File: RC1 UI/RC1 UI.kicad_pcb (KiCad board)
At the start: 2 copper layers, 99.1 x 97.2 mm, 59 parts, among them J1 KEYPAD, J2 RC1_UI_Port, J3 COM, J4 TAPE, M1 Mounting, M2 Mounting, M3 Mounting, M4 Mounting, Q1 2N3904, Q2 2N3904, Q3 2N3904, Q4 2N3904, Q5 2N3904, Q6 2N3904, U1 74LS138, U2 74LS138, U3 74LS01, U4 74LS00, U5 74LS04, U6 74LS244

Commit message: Gerber export
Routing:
- net VCC: track 411.6 -> 409.4 mm
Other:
- outline, holes or cut-outs redrawn
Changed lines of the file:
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@@
     (links 202)
     (no_connects 0)
-    (area 107.874999 36.754999 207.085001 134.060001)
+    (area 104.775 34.925 215.880001 140.970001)
     (thickness 1.6)
-    (drawings 147)
-    (tracks 1225)
+    (drawings 149)
+    (tracks 1228)
     (zones 0)
     (modules 59)
@@
     )
   )
+  (gr_line (start 202.565 133.985) (end 112.395 133.985) (angle 90) (layer Edge.Cuts) (width 0.15))
+  (gr_line (start 207.01 41.275) (end 207.01 129.54) (angle 90) (layer Edge.Cuts) (width 0.15))
+  (gr_line (start 107.95 129.54) (end 107.95 41.275) (angle 90) (layer Edge.Cuts) (width 0.15))
+  (gr_arc (start 202.565 129.54) (end 207.01 129.54) (angle 90) (layer Edge.Cuts) (width 0.15))
+  (gr_arc (start 112.395 129.54) (end 112.395 133.985) (angle 90) (layer Edge.Cuts) (width 0.15))
   (gr_text "00\n1C\n00\n1C" (at 173.99 114.3) (layer F.SilkS)
     (effects (font (size 1 1) (thickness 0.15)) (justify right))
@@
     (effects (font (size 1 1) (thickness 0.15)))
   )
-  (gr_line (start 107.95 133.985) (end 107.95 41.275) (angle 90) (layer Edge.Cuts) (width 0.15))
-  (gr_line (start 207.01 133.985) (end 207.01 41.275) (angle 90) (layer Edge.Cuts) (width 0.15))
-  (gr_line (start 107.95 133.985) (end 207.01 133.985) (angle 90) (layer Edge.Cuts) (width 0.15))
   (gr_text "6x 2N3904" (at 161.925 61.595) (layer B.SilkS)
     (effects (font (size 1 1) (thickness 0.15)) (justify mirror))
@@
   (gr_arc (start 112.395 41.275) (end 107.95 41.275) (angle 90) (layer Edge.Cuts) (width 0.15))
   (gr_arc (start 202.565 41.275) (end 202.565 36.83) (angle 90) (layer Edge.Cuts) (width 0.15))
+  (segment (start 206.375 130.175) (end 206.375 130.81) (width 0.25) (layer F.Cu) (net 1))
+  (segment (start 203.835 133.35) (end 203.2 133.35) (width 0.25) (layer F.Cu) (net 1))
+  (segment (start 206.375 130.81) (end 203.835 133.35) (width 0.25) (layer F.Cu) (net 1))
+  (segment (start 110.49 132.715) (end 111.125 133.35) (width 0.25) (layer B.Cu) (net 1))
+  (segment (start 111.125 133.35) (end 112.395 133.35) (width 0.25) (layer B.Cu) (net 1))
+  (via (at 112.395 133.35) (size 0.6) (drill 0.4) (layers F.Cu B.Cu) (net 1))
+  (segment (start 108.585 130.81) (end 110.49 132.715) (width 0.25) (layer B.Cu) (net 1))
   (segment (start 144.78 113.03) (end 137.16 113.03) (width 0.25) (layer B.Cu) (net 1))
   (segment (start 137.16 113.03) (end 136.525 113.665) (width 0.25) (layer B.Cu) (net 1))
@@
   (segment (start 194.31 100.965) (end 194.945 100.33) (width 0.25) (layer B.Cu) (net 1))
   (segment (start 194.31 109.22) (end 194.31 100.965) (width 0.25) (layer B.Cu) (net 1))
-  (segment (start 198.12 133.35) (end 205.74 133.35) (width 0.25) (layer F.Cu) (net 1))
+  (segment (start 198.12 133.35) (end 203.2 133.35) (width 0.25) (layer F.Cu) (net 1))
   (segment (start 195.58 111.125) (end 195.58 109.855) (width 0.25) (layer F.Cu) (net 1))
   (segment (start 196.215 111.76) (end 195.58 111.125) (width 0.25) (layer F.Cu) (net 1))
@@
   (segment (start 206.375 126.365) (end 206.375 112.395) (width 0.25) (layer B.Cu) (net 1))
   (via (at 206.375 126.365) (size 0.6) (drill 0.4) (layers F.Cu B.Cu) (net 1))
-  (segment (start 206.375 132.715) (end 206.375 126.365) (width 0.25) (layer F.Cu) (net 1))
-  (segment (start 205.74 133.35) (end 206.375 132.715) (width 0.25) (layer F.Cu) (net 1))
+  (segment (start 206.375 130.175) (end 206.375 126.365) (width 0.25) (layer F.Cu) (net 1))
   (segment (start 198.12 133.35) (end 196.85 133.35) (width 0.25) (layer F.Cu) (net 1))
   (segment (start 196.85 133.35) (end 162.56 133.35) (width 0.25) (layer F.Cu) (net 1))
@@
   (segment (start 125.73 133.35) (end 126.365 133.35) (width 0.25) (layer F.Cu) (net 1))
   (segment (start 126.365 133.35) (end 146.05 133.35) (width 0.25) (layer F.Cu) (net 1))
-  (segment (start 108.585 132.08) (end 108.585 132.715) (width 0.25) (layer B.Cu) (net 1))
-  (segment (start 109.22 133.35) (end 124.46 133.35) (width 0.25) (layer F.Cu) (net 1))
-  (via (at 109.22 133.35) (size 0.6) (drill 0.4) (layers F.Cu B.Cu) (net 1))
-  (segment (start 108.585 132.715) (end 109.22 133.35) (width 0.25) (layer B.Cu) (net 1))
+  (segment (start 112.395 133.35) (end 124.46 133.35) (width 0.25) (layer F.Cu) (net 1))
   (segment (start 112.395 72.39) (end 109.22 72.39) (width 0.25) (layer F.Cu) (net 1))
-  (segment (start 108.585 73.025) (end 108.585 132.08) (width 0.25) (layer B.Cu) (net 1))
+  (segment (start 108.585 73.025) (end 108.585 130.81) (width 0.25) (layer B.Cu) (net 1))
   (via (at 108.585 73.025) (size 0.6) (drill 0.4) (layers F.Cu B.Cu) (net 1))
   (segment (start 109.22 72.39) (end 108.585 73.025) (width 0.25) (layer F.Cu) (net 1))
@@
   (segment (start 118.745 93.345) (end 118.11 93.98) (width 0.25) (layer F.Cu) (net 32))
   (segment (start 114.935 102.87) (end 116.205 102.87) (width 0.25) (layer F.Cu) (net 32))
-  (segment (start 138.43 93.345) (end 140.335 93.345) (width 0.25) (layer F.Cu) (net 32) (status 2))
+  (segment (start 138.43 93.345) (end 140.335 93.345) (width 0.25) (layer F.Cu) (net 32))
   (segment (start 139.065 96.52) (end 134.62 92.075) (width 0.25) (layer B.Cu) (net 33))
   (via (at 134.62 92.075) (size 0.6) (drill 0.4) (layers F.Cu B.Cu) (net 33))
@@
   (segment (start 113.665 99.06) (end 115.57 99.06) (width 0.25) (layer F.Cu) (net 34))
   (segment (start 181.61 91.44) (end 182.88 90.17) (width 0.25) (layer F.Cu) (net 34))
-  (segment (start 132.715 91.44) (end 138.43 91.44) (width 0.25) (layer F.Cu) (net 34) (status 2))
+  (segment (start 132.715 91.44) (end 138.43 91.44) (width 0.25) (layer F.Cu) (net 34))
   (segment (start 138.43 91.44) (end 181.61 91.44) (width 0.25) (layer F.Cu) (net 34))
   (segment (start 137.795 97.79) (end 132.715 92.71) (width 0.25) (layer B.Cu) (net 35))

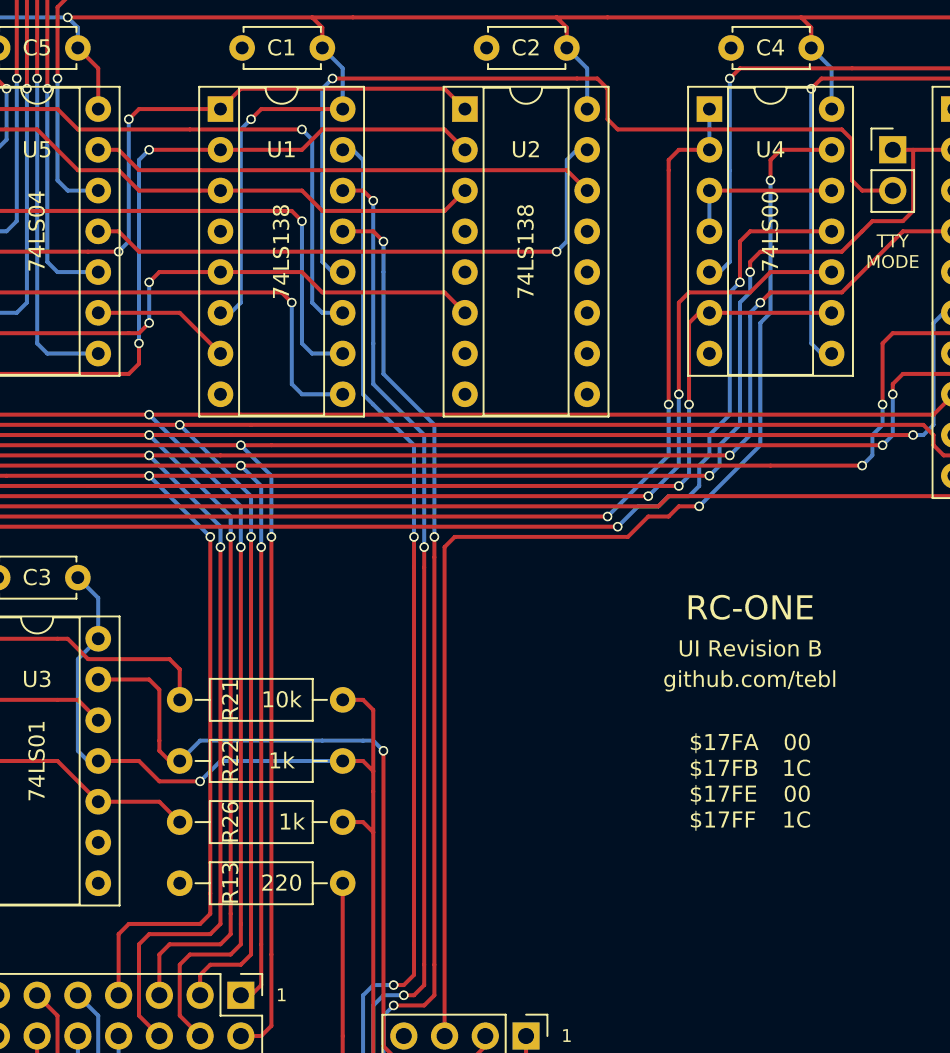
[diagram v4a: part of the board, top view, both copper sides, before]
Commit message: Added diodes to UI board
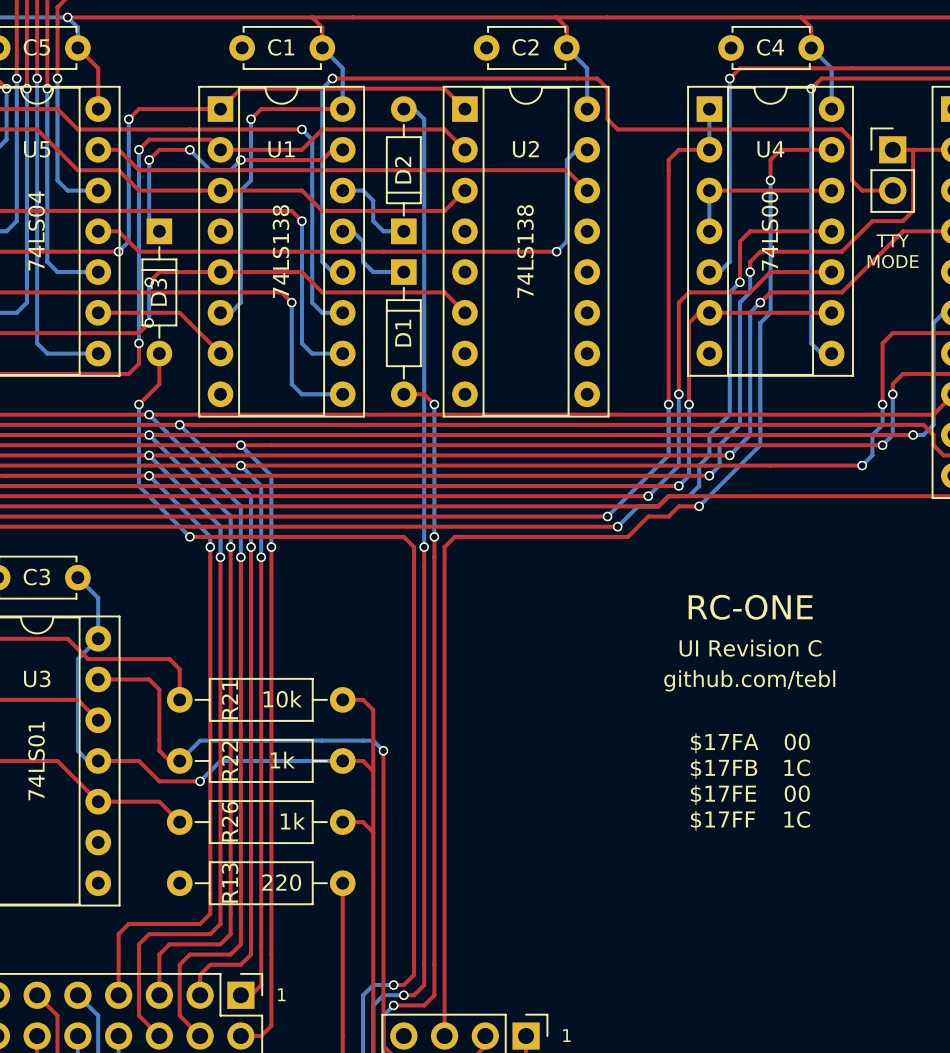
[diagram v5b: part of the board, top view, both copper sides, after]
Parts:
- added D1: 1n4148, Diodes_THT:D_DO-35_SOD27_P7.62mm_Horizontal, F.Cu at (148.6, 82.5)
- added D2: 1n4148, Diodes_THT:D_DO-35_SOD27_P7.62mm_Horizontal, F.Cu at (148.6, 80.0)
- added D3: 1n4148, Diodes_THT:D_DO-35_SOD27_P7.62mm_Horizontal, F.Cu at (133.3, 80.0)
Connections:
- U1 pad 13: /ROW2 -> Net-(D1-Pad1)
- U1 pad 14: /ROW1 -> Net-(D2-Pad1)
- U1 pad 15: /ROW0 -> Net-(D3-Pad1)
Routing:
- net Net-(D3-Pad1): track 0.00 -> 18.1 mm, vias 0 -> 3
- net /ROW2: track 80.7 -> 68.6 mm
- net Net-(D2-Pad1): track 0.00 -> 5.61 mm
- net Net-(D1-Pad1): track 0.00 -> 5.61 mm
- net /ROW1: track 82.5 -> 85.7 mm, vias 3 -> 2
- net /PB2: track 103.6 -> 104.5 mm
- net /ROW0: track 78.8 -> 79.4 mm, vias 2 -> 3
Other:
- board text added: "UI Revision C"
- board text removed: "UI Revision B"

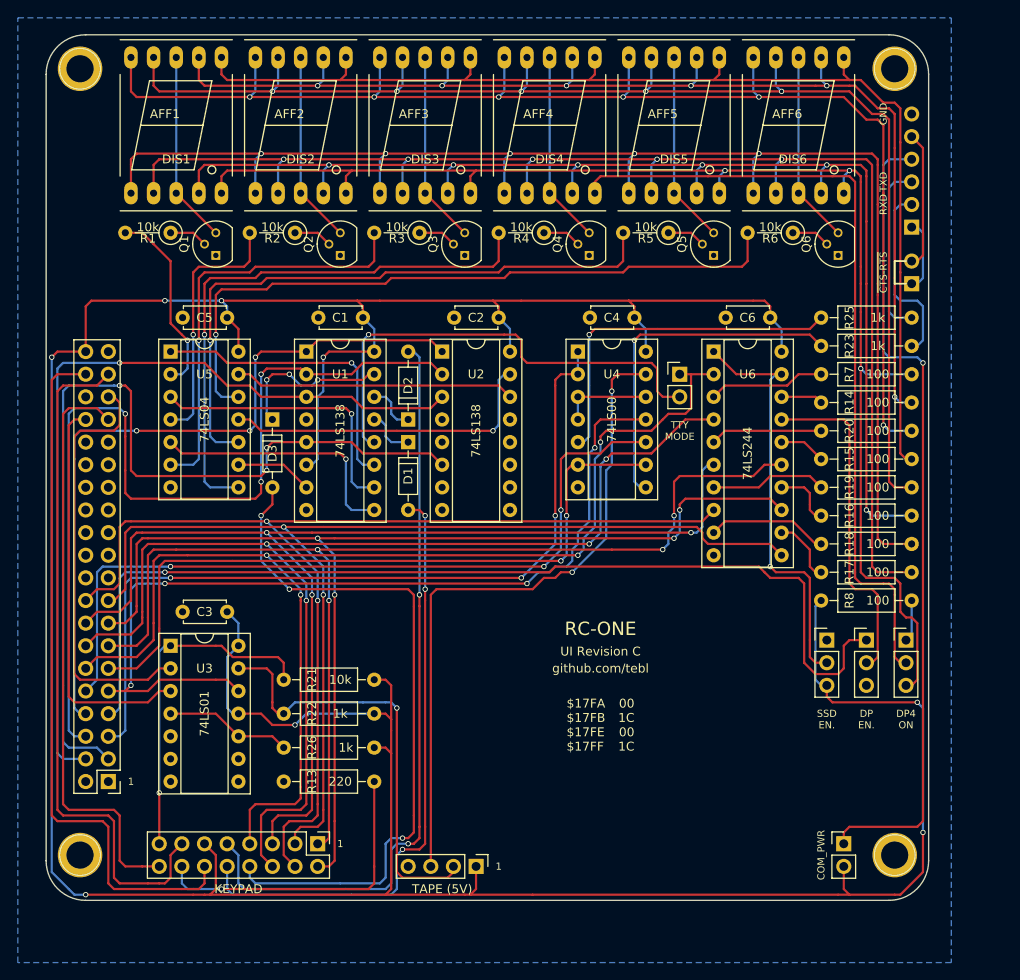
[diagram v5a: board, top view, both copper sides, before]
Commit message: Changed UI resistors to horizontal
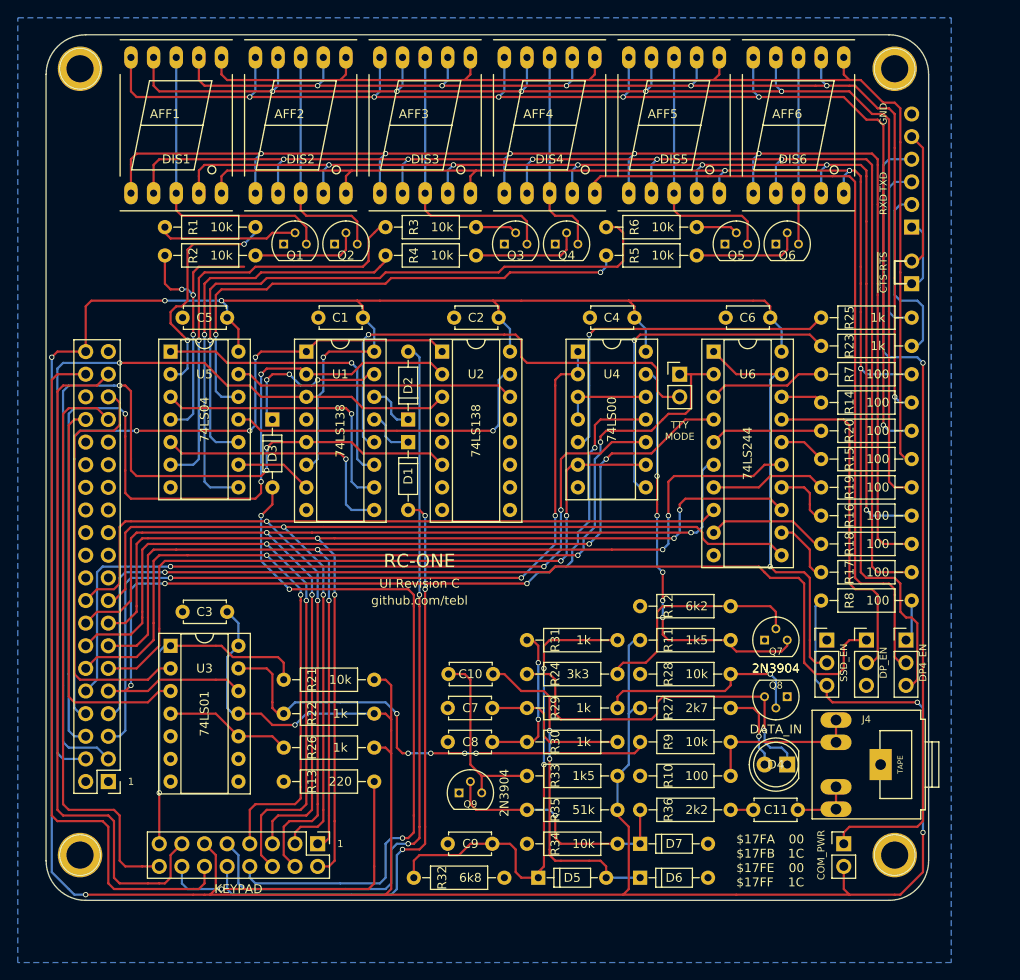
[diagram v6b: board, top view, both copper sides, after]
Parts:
- added C10: 500nF, Capacitors_THT:C_Disc_D4.7mm_W2.5mm_P5.00mm, F.Cu at (158.1, 108.6)
- added C11: 100nF, Capacitors_THT:C_Disc_D4.7mm_W2.5mm_P5.00mm, F.Cu at (187.3, 123.8)
- added C7: 50nF, Capacitors_THT:C_Disc_D4.7mm_W2.5mm_P5.00mm, F.Cu at (153.0, 112.4)
- added C8: 68nF, Capacitors_THT:C_Disc_D4.7mm_W2.5mm_P5.00mm, F.Cu at (153.0, 116.2)
- added C9: 50nF, Capacitors_THT:C_Disc_D4.7mm_W2.5mm_P5.00mm, F.Cu at (153.0, 127.6)
- added D4: DATA_IN, LEDs:LED_D5.0mm, F.Cu at (191.1, 118.7)
- added D5: 1n914, Diodes_THT:D_DO-35_SOD27_P7.62mm_Horizontal, F.Cu at (163.2, 131.4)
- added D6: 1n914, Diodes_THT:D_DO-35_SOD27_P7.62mm_Horizontal, F.Cu at (174.6, 131.4)
- added D7: 1n914, Diodes_THT:D_DO-35_SOD27_P7.62mm_Horizontal, F.Cu at (174.6, 127.6)
- added Q7: 2N3904, TO_SOT_Packages_THT:TO-92_Molded_Narrow, F.Cu at (188.6, 104.8)
- added Q8: 2N3904, TO_SOT_Packages_THT:TO-92_Molded_Narrow, F.Cu at (191.1, 111.1)
- added Q9: 2N3904, TO_SOT_Packages_THT:TO-92_Molded_Narrow, F.Cu at (154.3, 121.9)
- added R10: 100, Resistors_THT:R_Axial_DIN0207_L6.3mm_D2.5mm_P10.16mm_Horizontal, F.Cu at (184.8, 120.0)
- added R11: 1k5, Resistors_THT:R_Axial_DIN0207_L6.3mm_D2.5mm_P10.16mm_Horizontal, F.Cu at (184.8, 104.8)
- added R12: 6k2, Resistors_THT:R_Axial_DIN0207_L6.3mm_D2.5mm_P10.16mm_Horizontal, F.Cu at (184.8, 101.0)
- added R24: 3k3, Resistors_THT:R_Axial_DIN0207_L6.3mm_D2.5mm_P10.16mm_Horizontal, F.Cu at (161.9, 108.6)
- added R27: 2k7, Resistors_THT:R_Axial_DIN0207_L6.3mm_D2.5mm_P10.16mm_Horizontal, F.Cu at (184.8, 112.4)
- added R28: 10k, Resistors_THT:R_Axial_DIN0207_L6.3mm_D2.5mm_P10.16mm_Horizontal, F.Cu at (174.6, 108.6)
- added R29: 1k, Resistors_THT:R_Axial_DIN0207_L6.3mm_D2.5mm_P10.16mm_Horizontal, F.Cu at (161.9, 112.4)
- added R30: 1k, Resistors_THT:R_Axial_DIN0207_L6.3mm_D2.5mm_P10.16mm_Horizontal, F.Cu at (161.9, 116.2)
- added R31: 1k, Resistors_THT:R_Axial_DIN0207_L6.3mm_D2.5mm_P10.16mm_Horizontal, F.Cu at (172.1, 104.8)
- added R32: 6k8, Resistors_THT:R_Axial_DIN0207_L6.3mm_D2.5mm_P10.16mm_Horizontal, F.Cu at (149.2, 131.4)
- added R33: 1k5, Resistors_THT:R_Axial_DIN0207_L6.3mm_D2.5mm_P10.16mm_Horizontal, F.Cu at (161.9, 120.0)
- added R34: 10k, Resistors_THT:R_Axial_DIN0207_L6.3mm_D2.5mm_P10.16mm_Horizontal, F.Cu at (172.1, 127.6)
- added R35: 51k, Resistors_THT:R_Axial_DIN0207_L6.3mm_D2.5mm_P10.16mm_Horizontal, F.Cu at (172.1, 123.8)
- added R36: 2k2, Resistors_THT:R_Axial_DIN0207_L6.3mm_D2.5mm_P10.16mm_Horizontal, F.Cu at (174.6, 123.8)
- added R9: 10k, Resistors_THT:R_Axial_DIN0207_L6.3mm_D2.5mm_P10.16mm_Horizontal, F.Cu at (184.8, 116.2)
- J4: footprint Pin_Headers:Pin_Header_Straight_1x04_Pitch2.54mm -> TRS:Tayda_3.5mm_stereo_TRS_jack_A-853
- R1, R2, R3, R4, R5, R6: footprint Resistors_THT:R_Axial_DIN0207_L6.3mm_D2.5mm_P5.08mm_Vertical -> Resistors_THT:R_Axial_DIN0207_L6.3mm_D2.5mm_P10.16mm_Horizontal
- moved J4 45.3 mm to (200.0, 118.7)
- moved R6 11.1 mm to (181.0, 61.6)
- moved R4 8.03 mm to (156.2, 61.6)
- moved Q1 7.73 mm to (134.6, 60.3), turned to 0 degrees
- moved Q6 7.10 mm to (189.9, 60.3), turned to 0 degrees
- moved R3 6.38 mm to (156.2, 58.4)
- moved R2 5.12 mm to (131.4, 61.6)
- moved Q3 4.62 mm to (159.4, 60.3), turned to 0 degrees
- moved Q4 4.02 mm to (165.1, 60.3), turned to 0 degrees
- moved R5 3.24 mm to (181.0, 58.4)
- moved Q5 1.80 mm to (184.2, 60.3), turned to 0 degrees
- moved Q2 1.42 mm to (140.3, 60.3), turned to 0 degrees
- moved R1 0.90 mm to (121.3, 58.4), turned to 0 degrees
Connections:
- J4 pad 1: VCC -> GND
- J4 pad 2: Net-(J4-Pad2) -> /TAPE_EAR
- J4 pad 3: Net-(J4-Pad3) -> /TAPE_EAR
- J4 pad 4: GND -> /TAPE_MIC
- R22 pad 1: Net-(J4-Pad2) -> TO_TAPE
- U3 pad 13: Net-(J4-Pad2) -> TO_TAPE
- U4 pad 13: Net-(J4-Pad3) -> FROM_TAPE
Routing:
- net Net-(J4-Pad3): track 74.9 -> 0.00 mm, vias 2 -> 0
- net TO_TAPE: track 0.00 -> 56.1 mm, vias 0 -> 5
- net Net-(C9-Pad2): track 0.00 -> 54.5 mm, vias 0 -> 2
- net Net-(J4-Pad2): track 49.5 -> 0.00 mm, vias 1 -> 0
- net FROM_TAPE: track 0.00 -> 46.4 mm, vias 0 -> 5
- net Net-(D4-Pad1): track 0.00 -> 42.2 mm, vias 0 -> 1
- net Net-(C10-Pad1): track 0.00 -> 37.1 mm, vias 0 -> 2
- net VCC: track 409.4 -> 438.9 mm
- net Net-(D7-Pad1): track 0.00 -> 28.7 mm, vias 0 -> 1
- net Net-(Q7-Pad2): track 0.00 -> 26.1 mm
- net Net-(Q8-Pad2): track 0.00 -> 24.9 mm, vias 0 -> 1
- net Net-(C10-Pad2): track 0.00 -> 21.0 mm
- net /TAPE_MIC: track 0.00 -> 18.2 mm
- net /DIS6: track 78.0 -> 60.0 mm, vias 1 -> 2
- net Net-(C7-Pad2): track 0.00 -> 17.1 mm
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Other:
- board text added: "DP4_EN"
- board text added: "DP_EN"
- board text added: "FROM TAPE"
- board text added: "SSD_EN"
- board text added: "TAPE INTERFACE"
- board text added: "TO TAPE"
- board text removed: "7SEGMENT ENABLE"
- board text removed: "CONNECT PB6 TO DP"
- board text removed: "DP EN."
- board text removed: "DP4 ALWAYS ON"
- board text removed: "DP4 ON"
- board text removed: "SSD EN."
- board text removed: "TAPE (5V)"
- board text removed: "TAPE (TTL LEVEL)"
